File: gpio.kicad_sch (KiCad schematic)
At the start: 30 parts, among them Q1 AUIRF7316QTR, Q2 AUIRF7316QTR, Q3 AUIRF7316QTR, Q4 AUIRF7316QTR, U5 NPIC6C596ADJ, U6 PCF8574DWR

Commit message: WIP 5 FEB 2021
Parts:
- R35: footprint TestPoint:TestPoint_2Pads_Pitch2.54mm_Drill0.8mm -> Resistor_SMD:R_0805_2012Metric
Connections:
- net +3V3: now also U6.16 (Vcc)
- net GND: now also U6.1 (A0), U6.2 (A1), U6.3 (A2); no longer U6.7 (P3)
- net I_{1}: now also U6.4 (P0)
- net I_{2}: now also U6.5 (P1)
- net I_{3}: now also U6.6 (P2)
- net I_{4}: now also U6.7 (P3)
- net I_{5}: now also U6.12 (P7)
- net I_{6}: now also U6.11 (P6)
- net I_{7}: now also U6.10 (P5)
- net I_{8}: now also U6.9 (P4)
- net SCL: now also U6.14 (SCL)
- net SDA: now also U6.15 (SDA)
- net ~INT: now also U6.13 (~INT)
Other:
- moved on the sheet: U6
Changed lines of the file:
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@@
   (junction (at 81.28 119.38) (diameter 0.9144) (color 0 0 0 0))
   (junction (at 87.63 119.38) (diameter 0.9144) (color 0 0 0 0))
-  (junction (at 115.57 36.83) (diameter 0.9144) (color 0 0 0 0))
   (junction (at 115.57 38.1) (diameter 0.9144) (color 0 0 0 0))
-  (junction (at 115.57 39.37) (diameter 0.9144) (color 0 0 0 0))
   (junction (at 115.57 40.64) (diameter 0.9144) (color 0 0 0 0))
   (junction (at 115.57 53.34) (diameter 0.9144) (color 0 0 0 0))
-  (junction (at 115.57 54.61) (diameter 0.9144) (color 0 0 0 0))
   (junction (at 179.07 68.072) (diameter 0.9144) (color 0 0 0 0))
   (junction (at 179.07 94.742) (diameter 0.9144) (color 0 0 0 0))
@@
     (stroke (width 0) (type solid) (color 0 0 0 0))
   )
-  (wire (pts (xy 115.57 36.83) (xy 115.57 35.56))
-    (stroke (width 0) (type solid) (color 0 0 0 0))
-  )
-  (wire (pts (xy 115.57 38.1) (xy 115.57 36.83))
-    (stroke (width 0) (type solid) (color 0 0 0 0))
-  )
-  (wire (pts (xy 115.57 39.37) (xy 115.57 38.1))
-    (stroke (width 0) (type solid) (color 0 0 0 0))
-  )
-  (wire (pts (xy 115.57 40.64) (xy 115.57 39.37))
-    (stroke (width 0) (type solid) (color 0 0 0 0))
-  )
-  (wire (pts (xy 115.57 41.91) (xy 115.57 40.64))
-    (stroke (width 0) (type solid) (color 0 0 0 0))
-  )
-  (wire (pts (xy 115.57 53.34) (xy 115.57 52.07))
+  (wire (pts (xy 115.57 35.56) (xy 115.57 38.1))
+    (stroke (width 0) (type solid) (color 0 0 0 0))
+  )
+  (wire (pts (xy 115.57 38.1) (xy 115.57 40.64))
+    (stroke (width 0) (type solid) (color 0 0 0 0))
+  )
+  (wire (pts (xy 115.57 40.64) (xy 115.57 53.34))
     (stroke (width 0) (type solid) (color 0 0 0 0))
   )
@@
       (effects (font (size 1.27 1.27)) (justify left))
     )
-    (property "Footprint" "TestPoint:TestPoint_2Pads_Pitch2.54mm_Drill0.8mm" (id 2) (at 228.092 74.422 90)
+    (property "Footprint" "Resistor_SMD:R_0805_2012Metric" (id 2) (at 228.092 74.422 90)
       (effects (font (size 1.27 1.27)) hide)
     )
@@
     )
   )
-  (symbol (lib_id "symbols:PCF8574DWR") (at 107.95 45.72 0) (mirror y) (unit 1)
-    (in_bom yes) (on_board yes)
-    (property "Reference" "U6" (id 0) (at 107.315 30.2065 0))
-    (property "Value" "PCF8574DWR" (id 1) (at 107.315 32.5052 0))
-    (property "Footprint" "Package_SO:SOIC-16W_7.5x10.3mm_P1.27mm" (id 2) (at 111.76 31.75 0)
-      (effects (font (size 1.27 1.27)) hide)
-    )
-    (property "Datasheet" "https://www.ti.com/lit/ds/symlink/pcf8574.pdf?HQS=dis-dk-null-digikeymode-dsf-pf-null-wwe&ts=1609224079098" (id 3) (at 111.76 31.75 0)
-      (effects (font (size 1.27 1.27)) hide)
-    )
-    (property "Vendor" "Digikey" (id 4) (at 107.95 45.72 0)
-      (effects (font (size 1.27 1.27)) hide)
-    )
-    (property "Vendor Part" "296-13108-1-ND" (id 5) (at 107.95 45.72 0)
-      (effects (font (size 1.27 1.27)) hide)
-    )
-    (property "Manufacturer" "Texas Instruments" (id 6) (at 107.95 45.72 0)
-      (effects (font (size 1.27 1.27)) hide)
-    )
-    (property "Manufacturer Part" "PCF8574DWR" (id 7) (at 107.95 45.72 0)
-      (effects (font (size 1.27 1.27)) hide)
-    )
+  (symbol (lib_id "symbols:PCF8574DWR") (at 106.68 44.45 0) (mirror y) (unit 1)
+    (in_bom yes) (on_board yes)
+    (property "Reference" "U6" (id 0) (at 106.045 28.9365 0))
+    (property "Value" "PCF8574DWR" (id 1) (at 106.045 31.2352 0))
+    (property "Footprint" "Package_SO:SOIC-16W_7.5x10.3mm_P1.27mm" (id 2) (at 110.49 30.48 0)
+      (effects (font (size 1.27 1.27)) hide)
+    )
+    (property "Datasheet" "https://www.ti.com/lit/ds/symlink/pcf8574.pdf?HQS=dis-dk-null-digikeymode-dsf-pf-null-wwe&ts=1609224079098" (id 3) (at 110.49 30.48 0)
+      (effects (font (size 1.27 1.27)) hide)
+    )
+    (property "Vendor" "Digikey" (id 4) (at 106.68 44.45 0)
+      (effects (font (size 1.27 1.27)) hide)
+    )
+    (property "Vendor Part" "296-13108-1-ND" (id 5) (at 106.68 44.45 0)
+      (effects (font (size 1.27 1.27)) hide)
+    )
+    (property "Manufacturer" "Texas Instruments" (id 6) (at 106.68 44.45 0)
+      (effects (font (size 1.27 1.27)) hide)
+    )
+    (property "Manufacturer Part" "PCF8574DWR" (id 7) (at 106.68 44.45 0)
+      (effects (font (size 1.27 1.27)) hide)
+    )

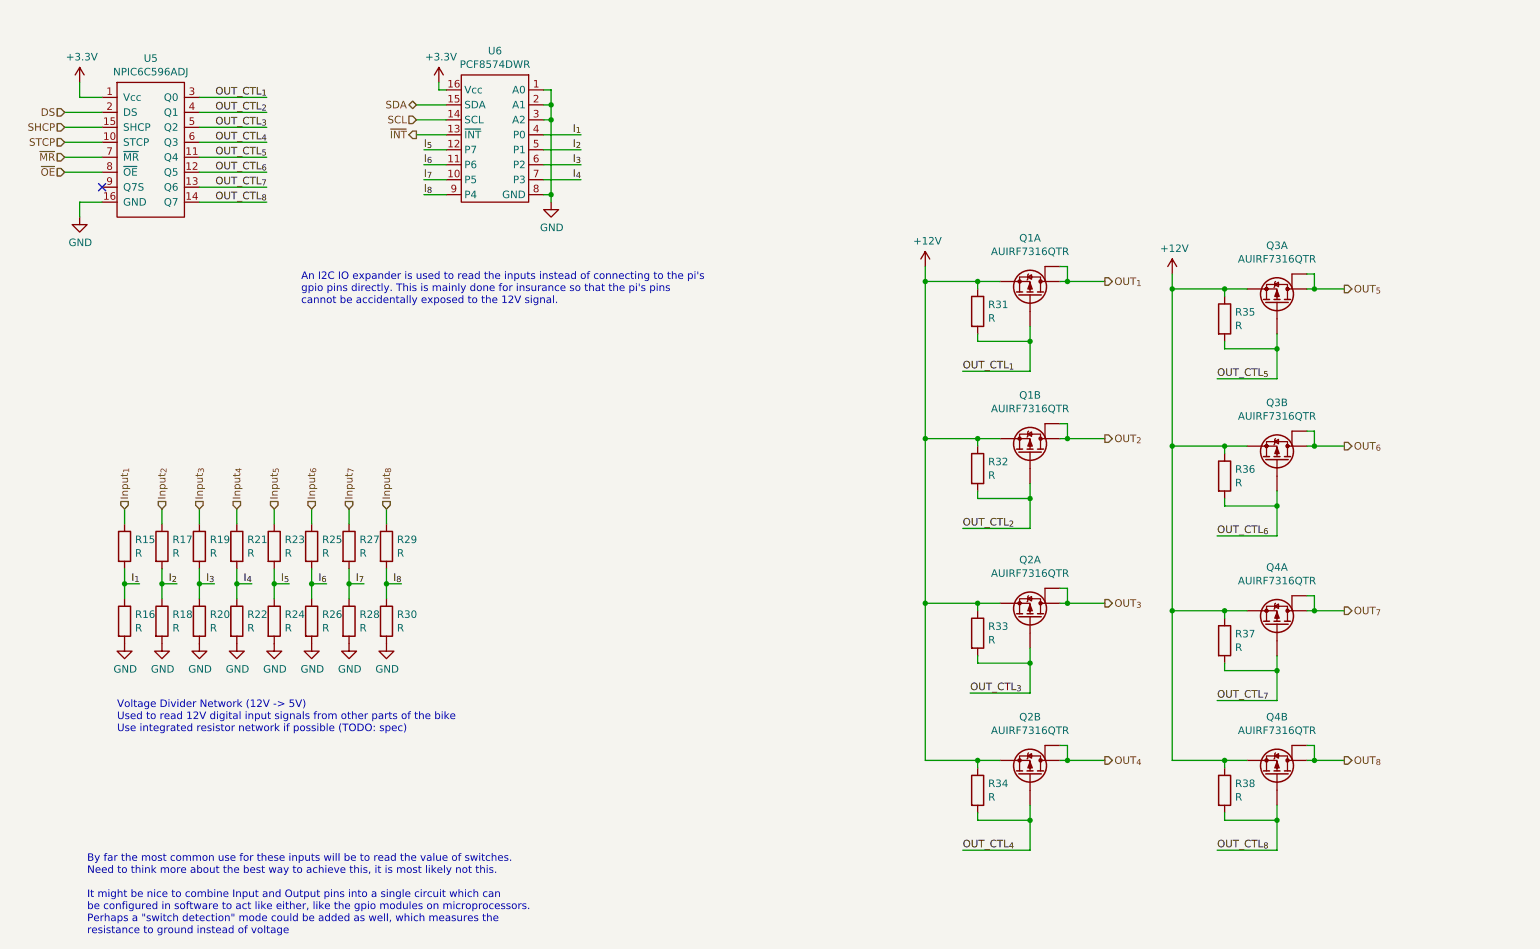
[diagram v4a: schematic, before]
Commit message: switched to networked resistors on GPIO system
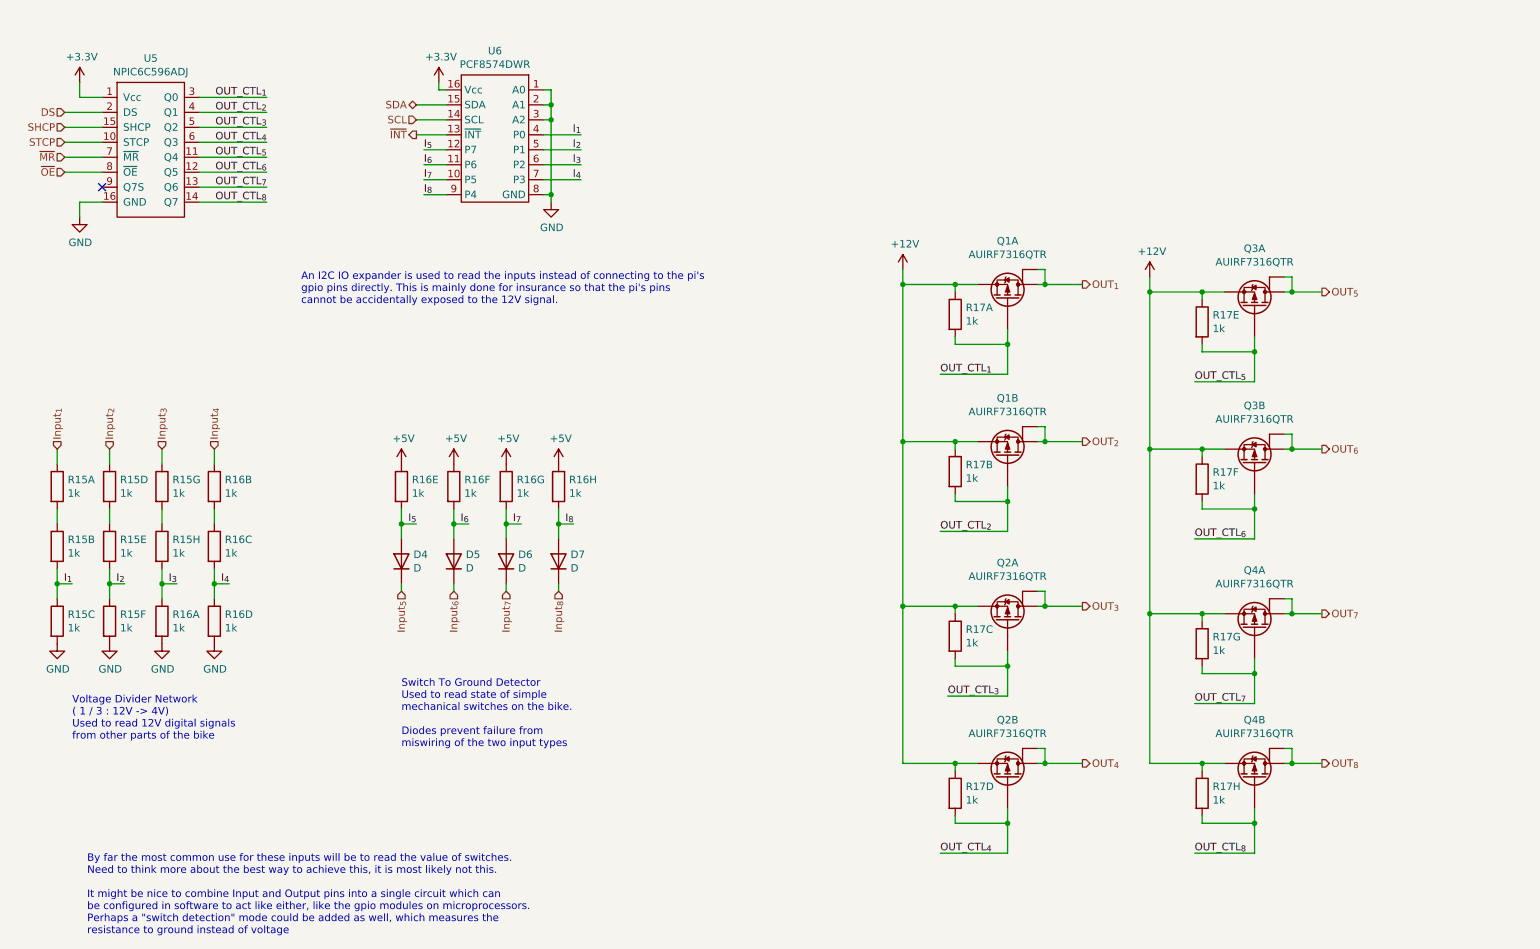
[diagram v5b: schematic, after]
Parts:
- removed R15, R16, R17, R18, R19, R20, R21, R22, R23, R24, R25, R26, R27, R28, R29, R30, R31, R32, R33, R34, R35, R36, R37, R38: R, Resistor_SMD:R_0805_2012Metric, symbol Device:R
- added D4, D5, D6, D7: D, symbol Device:D
- added R15, R16, R17: CTS-766161102GP, Package_SO:SOIC-16_3.9x9.9mm_P1.27mm, symbol symbols:CTS-766161102GP
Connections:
- net +12V: now also R17.1, R17.2, R17.3, R17.4, R17.5, R17.6, R17.7, R17.8
- net GND: now also R15.11, R15.14, R16.13, R16.16
- net I_{1}: now also R15.15, R15.3
- net I_{2}: now also R15.12, R15.6
- net I_{3}: now also R15.9, R16.1
- net I_{4}: now also R16.14, R16.4
- net I_{5}: now also D4.2 (A), R16.12
- net I_{6}: now also D5.2 (A), R16.11
- net I_{7}: now also D6.2 (A), R16.10
- net I_{8}: now also D7.2 (A), R16.9
- net Input_{1}: now also R15.1
- net Input_{2}: now also R15.4
- net Input_{3}: now also R15.7
- net Input_{4}: now also R16.2
- net Input_{5}: now also D4.1 (K)
- net Input_{6}: now also D5.1 (K)
- net Input_{7}: now also D6.1 (K)
- net Input_{8}: now also D7.1 (K)
- net OUT_CTL_{1}: now also R17.16
- net OUT_CTL_{2}: now also R17.15
- net OUT_CTL_{3}: now also R17.14
- net OUT_CTL_{4}: now also R17.13
- net OUT_CTL_{5}: now also R17.12
- net OUT_CTL_{6}: now also R17.11
- net OUT_CTL_{7}: now also R17.10
- net OUT_CTL_{8}: now also R17.9
- new net: R15.13, R15.5
- new net: R15.16, R15.2
- new net: R16.15, R16.3
- new net: R15.10, R15.8
- new net +5V: R16.5, R16.6, R16.7, R16.8
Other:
- note added: "Switch To Ground Detector Used to read state of simple mechanical switches on the bike. Diodes prevent failure from miswiring of the two input types"
- note added: "Voltage Divider Network ( 1 / 3 : 12V -> 4V) Used to read 12V digital signals from other parts of the bike"
- note removed: "Voltage Divider Network (12V -> 5V) Used to read 12V digital input signals from other parts of the bike Use integrated resistor network if possible (TODO: spec)"
- moved on the sheet: Q1A, Q1B, Q2A, Q2B, Q3A, Q3B, Q4A, Q4B

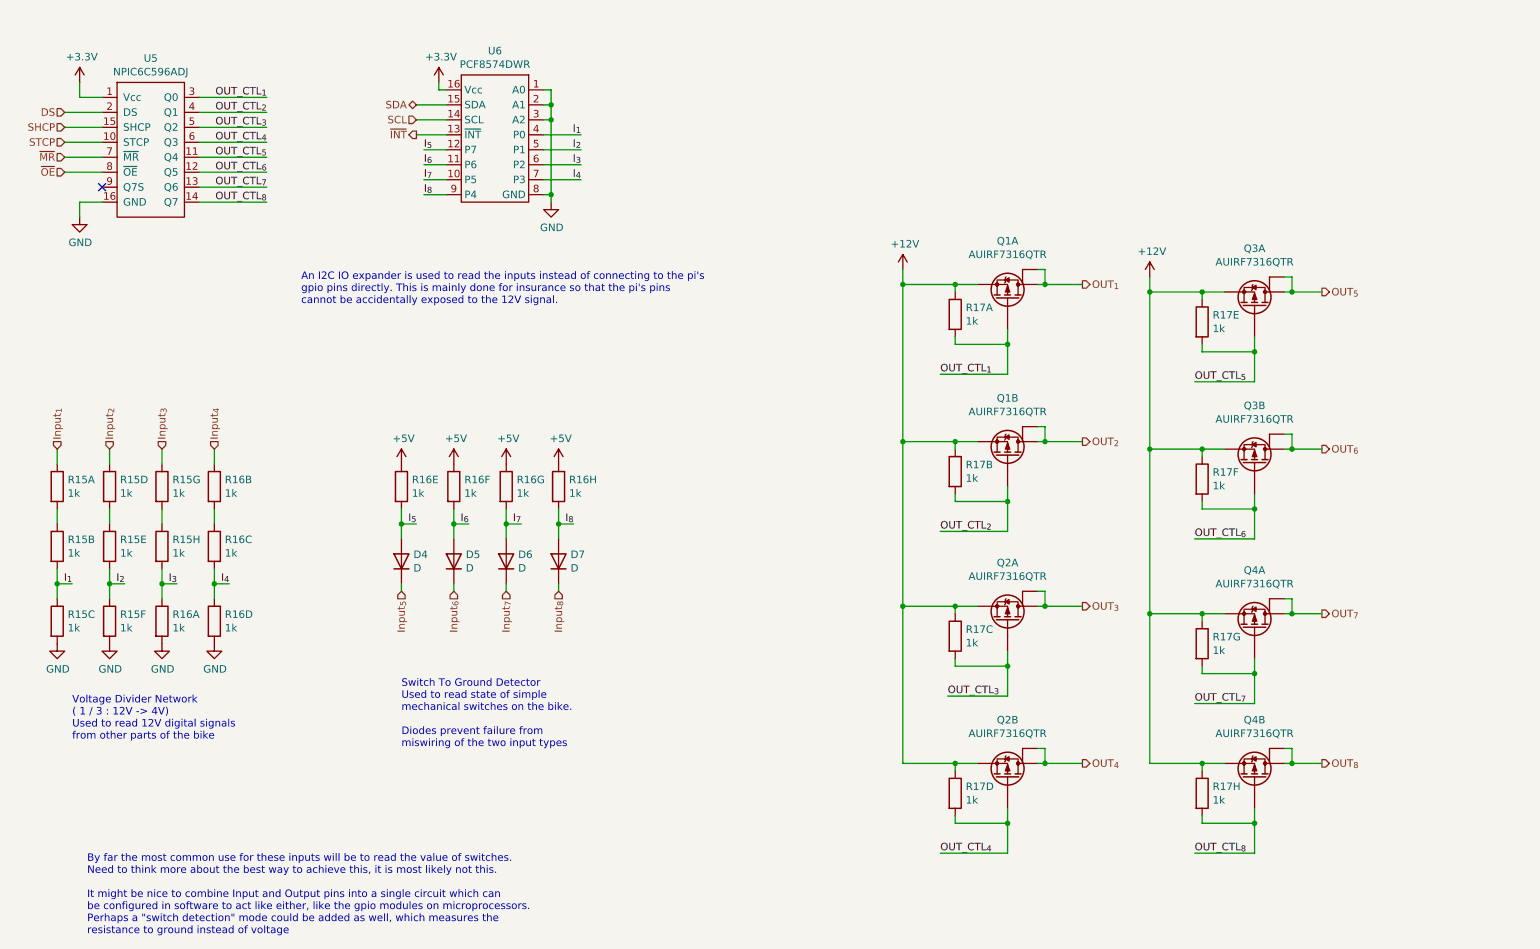
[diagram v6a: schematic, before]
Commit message: more layout: power supply and gpio
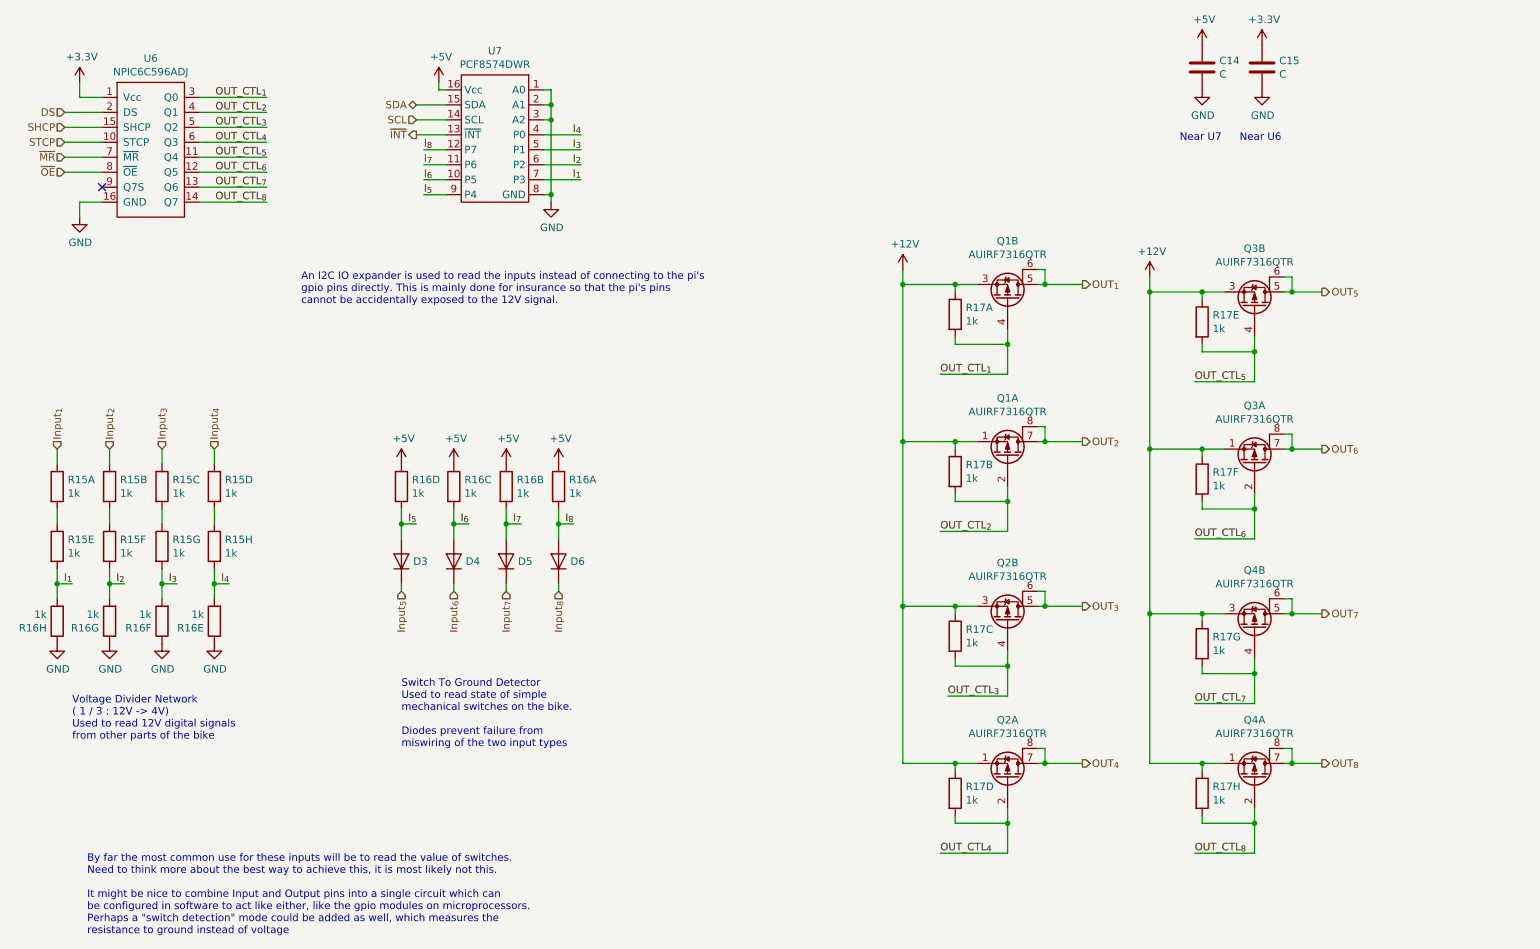
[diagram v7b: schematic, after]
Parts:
- removed D4, D5, D6, D7: D, symbol Device:D
- added C14, C15: C, Capacitor_SMD:C_0805_2012Metric, symbol Device:C
- added D3, D4, D5, D6: Diode, Diode_SMD:D_SOD-123F, symbol symbols:Diode
- renumbered R16 to R15, R15 to R16, U5 to U6, U6 to U7
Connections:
- net +12V: now also Q1.1 (S1), Q1.3 (S2), Q2.1 (S1), Q2.3 (S2), Q3.1 (S1), Q3.3 (S2), Q4.1 (S1), Q4.3 (S2); no longer Q1.1 (S), Q1.3 (S), Q2.1 (S), Q2.3 (S), Q3.1 (S), Q3.3 (S), Q4.1 (S), Q4.3 (S)
- net +3V3: now also C15.1; no longer U7.16 (Vcc)
- net +5V: now also R16.1, R16.2, R16.3, R16.4, U7.16 (Vcc), C14.1; no longer R16.5, R16.6, R16.7, R16.8
- net GND: now also R16.5, R16.6, R16.7, R16.8, C14.2, C15.2; no longer R16.11, R16.13, R16.14, R16.16
- net I_{1}: now also R15.12, R16.9, U7.7 (P3); no longer R15.15, R16.3, U7.4 (P0)
- net I_{2}: now also R15.11, R16.10, U7.6 (P2); no longer R15.12, R16.6, U7.5 (P1)
- net I_{3}: now also R15.10, R16.11, U7.5 (P1); no longer R15.9, R16.1, U7.6 (P2)
- net I_{4}: now also R15.9, R16.12, U7.4 (P0); no longer R15.14, R16.4, U7.7 (P3)
- net I_{5}: now also R16.13, U7.9 (P4), D3.2 (A); no longer R16.12, U7.12 (P7)
- net I_{6}: now also R16.14, U7.10 (P5), D4.2 (A); no longer R16.11, U7.11 (P6)
- net I_{7}: now also R16.15, U7.11 (P6), D5.2 (A); no longer R16.10, U7.10 (P5)
- net I_{8}: now also R16.16, U7.12 (P7), D6.2 (A); no longer R16.9, U7.9 (P4)
- net Input_{2}: now also R15.2; no longer R15.4
- net Input_{3}: now also R15.3; no longer R15.7
- net Input_{4}: now also R15.4; no longer R15.2
- net Input_{5}: now also D3.1 (K)
- net Input_{6}: now also D4.1 (K)
- net Input_{7}: now also D5.1 (K)
- net Input_{8}: now also D6.1 (K)
- net OUT_CTL_{1}: now also Q1.4 (G2); no longer Q1.2 (G)
- net OUT_CTL_{2}: now also Q1.2 (G1); no longer Q1.4 (G)
- net OUT_CTL_{3}: now also Q2.4 (G2); no longer Q2.2 (G)
- net OUT_CTL_{4}: now also Q2.2 (G1); no longer Q2.4 (G)
- net OUT_CTL_{5}: now also Q3.4 (G2); no longer Q3.2 (G)
- net OUT_CTL_{6}: now also Q3.2 (G1); no longer Q3.4 (G)
- net OUT_CTL_{7}: now also Q4.4 (G2); no longer Q4.2 (G)
- net OUT_CTL_{8}: now also Q4.2 (G1); no longer Q4.4 (G)
- net OUT_{1}: now also Q1.5 (D2); no longer Q1.7 (D)
- net OUT_{2}: now also Q1.7 (D1); no longer Q1.5 (D)
- net OUT_{3}: now also Q2.5 (D2); no longer Q2.7 (D)
- net OUT_{4}: now also Q2.7 (D1); no longer Q2.5 (D)
- net OUT_{5}: now also Q3.5 (D2); no longer Q3.7 (D)
- net OUT_{6}: now also Q3.7 (D1); no longer Q3.5 (D)
- net OUT_{7}: now also Q4.5 (D2); no longer Q4.7 (D)
- net OUT_{8}: now also Q4.7 (D1); no longer Q4.5 (D)
- net at R15.16: now also R15.5; no longer R15.2
- new net: R15.15, R15.6
- new net: R15.13, R15.8
- new net: R15.14, R15.7
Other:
- note added: "Near U6"
- note added: "Near U7"
- moved on the sheet: R16A, R16B, R16C, R16D, R16E, R16F, R16G, R16H

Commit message: Finished trace routing
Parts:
- renumbered C14 to C23, C15 to C24, D3 to D5, D4 to D6, D5 to D7, D6 to D8, Q1 to Q3, Q2 to Q4, Q3 to Q5, Q4 to Q6, R17 to R26, U6 to U7, U7 to U8
